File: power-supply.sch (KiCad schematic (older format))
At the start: 91 parts, among them IC1 TPS54561, J12 S2B-PH-K-S_LF__SN_, Q1 IRLML6402TRPBF, Q10 2N7002, Q11 2N7002, Q2 IRLML6402TRPBF, Q3 IRLML6402TRPBF, Q4 IRLML6402TRPBF, Q5 IRLML6402TRPBF, Q6 IRLML6402TRPBF, Q7 2N7002, Q8 2N7002, Q9 2N7002, U10 TPS62823DLCT, U11 TPS62823DLCT, U12 TPS62823DLCT, U13 TPS62823DLCT, U15 SN74LVC1G08DCKR, U16 SN74LS08DBR, U9 LM3881MME_NOPB

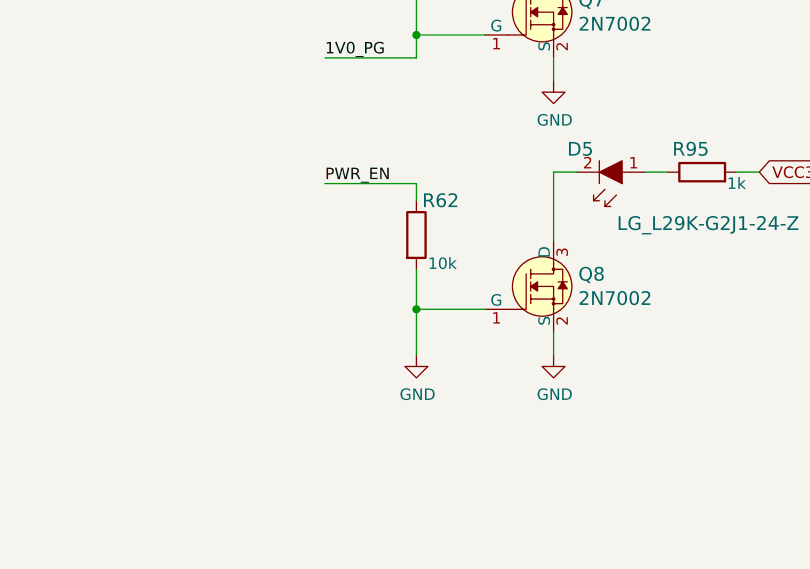
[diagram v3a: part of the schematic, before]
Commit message: Added power sequencer component placement, minor fixes in schematics
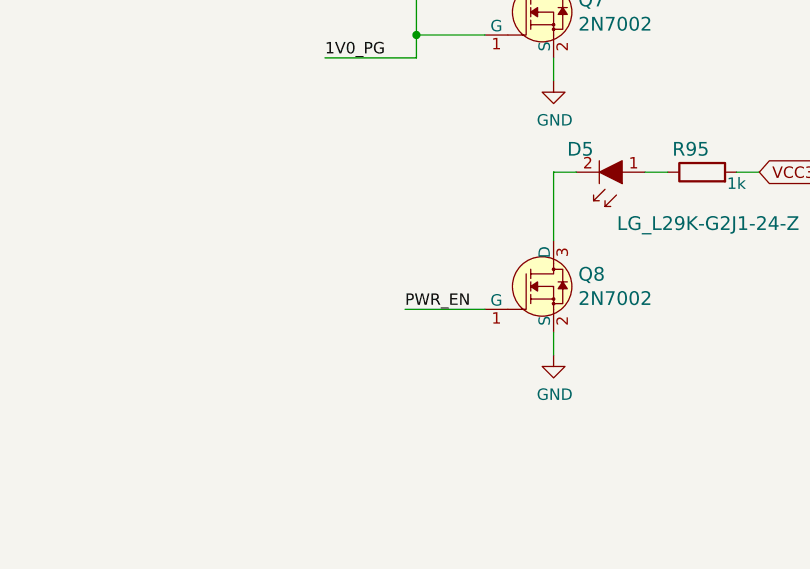
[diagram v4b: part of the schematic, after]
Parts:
- removed R62: R_10k_0402, artix-dc-scm-footprints:0402-res, symbol artix-dc-scm:R_10k_0402
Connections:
- wire segments 340 -> 336
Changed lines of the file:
@@
 AR Path="/5FD86BEB/60965625" Ref="U16"  Part="1"
 F 0 "U16" H 4175 9375 60  0000 C CNN
-F 1 "SN74LS08DBR" H 4050 9250 60  0000 C CNN
+F 1 "SN74LS08DBR" H 5250 9150 60  0000 C CNN
 F 2 "artix-dc-scm-footprints:SOP65P775X265-14N" H 4675 9075 60  0001 L CNN
 F 3 "http://www.ti.com/general/docs/suppproductinfo.tsp?distId=10&gotoUrl=http%3A%2F%2Fwww.ti.com%2Flit%2Fgpn%2Fsn74ls08" H 4675 9175 60  0001 L CNN
@@
 	10250 6775 10250 6675
 Wire Wire Line
-	9650 7775 9950 7775
-Wire Wire Line
 	10250 7175 10250 7475
-$Comp
-L artix-dc-scm:R_10k_0402 R62
-U 1 1 60986E26
-P 9650 7450
-F 0 "R62" V 9500 7475 60  0000 L CNN
-F 1 "R_10k_0402" H 9650 7300 60  0001 C CNN
-F 2 "artix-dc-scm-footprints:0402-res" H 9850 7650 60  0001 L CNN
-F 3 "" H 9650 7450 50  0001 C CNN
-F 4 "VISHAY" H 9850 7850 60  0001 L CNN "Manufacturer"
-F 5 "CRCW040210K0FKEDHP" H 9850 7750 60  0001 L CNN "MPN"
-F 6 "10k" V 9775 7500 50  0000 L CNN "Val"
-	1    9650 7450
-	0    1    1    0
-$EndComp
-Wire Wire Line
-	9650 7225 9650 7300
-Wire Wire Line
-	9650 7600 9650 7775
 $Comp
 L artix-dc-scm:LG_L29K-G2J1-24-Z D5
@@
 Wire Wire Line
 	11050 7175 11150 7175
-Connection ~ 9650 7775
 $Comp
 L artix-dc-scm:2N7002 Q8
@@
 Wire Wire Line
 	10250 7975 10250 7875
-Text Label 9250 7225 0    50   ~ 0
+Text Label 9600 7775 0    50   ~ 0
 PWR_EN
-Wire Wire Line
-	9250 7225 9650 7225
-$Comp
-L artix-dc-scm:GND #PWR0108
-U 1 1 60986E55
-P 9650 7975
-F 0 "#PWR0108" H 9650 7725 50  0001 C CNN
-F 1 "GND" H 9655 7802 50  0000 C CNN
-F 2 "" H 9650 7975 50  0001 C CNN
-F 3 "" H 9650 7975 50  0001 C CNN
-	1    9650 7975
-	1    0    0    -1
-$EndComp
-Wire Wire Line
-	9650 7775 9650 7975
 Wire Wire Line
 	9650 6575 9650 6675
@@
 Text GLabel 1125 9175 1    50   Input ~ 0
 VCC3V3
+Wire Wire Line
+	9950 7775 9600 7775
 $EndSCHEMATC

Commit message: Updated RoT and FLASH connections
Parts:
- renumbered R99 to R62
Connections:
- net labels added: ROT_RDY\ROT_GPIO0
- net labels removed: ROT_RDY
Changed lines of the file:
@@
 Text GLabel 4675 8875 2    50   Input ~ 0
 HPM_STBY_EN
-Text GLabel 4175 8775 0    50   Input ~ 0
-ROT_RDY
 Wire Wire Line
 	9725 2300 9650 2300
@@
 External 12V supply
 $Comp
-L artix-dc-scm:R_1k_0402 R99
+L artix-dc-scm:R_1k_0402 R62
 U 1 1 6003348A
 P 1125 9500
-F 0 "R99" V 1080 9570 60  0000 L CNN
+F 0 "R62" V 1080 9570 60  0000 L CNN
 F 1 "R_1k_0402" H 1125 9350 60  0001 C CNN
 F 2 "artix-dc-scm-footprints:0402-res" H 1325 9700 60  0001 L CNN
@@
 Wire Wire Line
 	9950 7775 9600 7775
+Text GLabel 4175 8775 0    50   Input ~ 0
+ROT_RDY\ROT_GPIO0
 $EndSCHEMATC

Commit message: Fixes after review (pin connections)
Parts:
- removed R77: R_124k_0402, artix-dc-scm-footprints:0402-res, symbol artix-dc-scm:R_124k_0402
- added R77: R_66k5_0402, antmicro-footprints:0402-res, symbol artix-dc-scm:R_66k5_0402
- added TP10, TP11, TP7, TP8, TP9: TP_SMD1MM, artix-dc-scm-footprints:Testpoint_smd_1mm, symbol artix-dc-scm:TP_SMD1MM
- U15: footprint artix-dc-scm-footprints:SC-70-5 -> antmicro-footprints:SC-70-5
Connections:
- wire segments 336 -> 333
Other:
- note removed: "SOURCE:LPDDR4 board"
- note removed: "TODO: calculate correct value for ??? resistor"
- note removed: "To CHECK"
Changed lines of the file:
@@
 Wire Wire Line
 	14325 2750 14625 2750
-Text Notes 14625 2300 0    50   ~ 0
+Text Notes 14600 2425 0    50   ~ 0
 3.3V/3A
 NoConn ~ -625 5725
@@
 Wire Wire Line
 	6600 3200 6600 3475
-Text GLabel 6600 2825 1    50   Input ~ 0
+Text GLabel 6600 2775 1    50   Input ~ 0
 VCC5V0
 Wire Wire Line
-	6600 2900 6600 2825
+	6600 2900 6600 2850
 $Comp
 L artix-dc-scm:WE_7447798720 L1
@@
 Wire Wire Line
 	12375 2750 12375 2800
-Text GLabel 12350 2350 0    50   Input ~ 0
-VCC5V0
-Wire Wire Line
-	12375 2350 12350 2350
 Wire Wire Line
 	12375 2350 12375 2750
@@
 Wire Wire Line
 	15275 3300 15275 3550
-Text GLabel 14925 2375 0    50   Input ~ 0
+Text GLabel 14975 2375 1    50   Input ~ 0
 VCC3V3
 Wire Wire Line
-	14975 2375 14925 2375
-Wire Wire Line
 	14975 2375 14975 2750
-Text Notes 4725 2725 0    50   ~ 0
-SOURCE:LPDDR4 board
 Text Notes 12725 3500 0    50   ~ 0
 SOURCE:Trelis board
@@
 Wire Wire Line
 	12400 4900 12400 4950
-Text GLabel 12375 4500 0    50   Input ~ 0
-VCC5V0
-Wire Wire Line
-	12400 4500 12375 4500
 Wire Wire Line
 	12400 4500 12400 4900
@@
 Wire Wire Line
 	15300 5450 15300 5700
-Text GLabel 14950 4525 0    50   Input ~ 0
+Text GLabel 15000 4525 1    50   Input ~ 0
 VCC1V8
-Wire Wire Line
-	15000 4525 14950 4525
 Wire Wire Line
 	15000 4525 15000 4900
@@
 Wire Wire Line
 	12450 6725 12450 6775
-Text GLabel 12425 6325 0    50   Input ~ 0
-VCC5V0
-Wire Wire Line
-	12450 6325 12425 6325
 Wire Wire Line
 	12450 6325 12450 6725
@@
 Wire Wire Line
 	15350 7275 15350 7525
-Text GLabel 15000 6350 0    50   Input ~ 0
+Text GLabel 15050 6350 1    50   Input ~ 0
 VCC1V35
-Wire Wire Line
-	15050 6350 15000 6350
 Wire Wire Line
 	15050 6350 15050 6725
@@
 	1    0    0    -1
 $EndComp
-Text Notes 1900 6825 0    118  ~ 0
-To CHECK
 Text Label 3000 9775 2    50   ~ 0
 VCCINT_EN
@@
 	1    0    0    -1
 $EndComp
-Text Notes 9075 975  0    118  ~ 0
+Text Notes 9525 1825 0    118  ~ 0
 PWR_LED Indicators
 Wire Notes Line
@@
 Wire Wire Line
 	15325 9000 15325 9250
-Text GLabel 14975 8075 0    50   Input ~ 0
+Text GLabel 15025 8075 1    50   Input ~ 0
 VCC1V0
-Wire Wire Line
-	15025 8075 14975 8075
 Wire Wire Line
 	15025 8075 15025 8450
@@
 Wire Wire Line
 	13875 8450 13825 8450
-$Comp
-L artix-dc-scm:R_124k_0402 R77
-U 1 1 63A59281
-P 14675 8675
-F 0 "R77" V 14630 8745 60  0000 L CNN
-F 1 "R_124k_0402" H 14675 8525 60  0001 C CNN
-F 2 "artix-dc-scm-footprints:0402-res" H 14875 8875 60  0001 L CNN
-F 3 "" H 14675 8675 50  0001 C CNN
-F 4 "WALSIN" H 14875 9075 60  0001 L CNN "Manufacturer"
-F 5 "WR04X1243FTL" H 14875 8975 60  0001 L CNN "MPN"
-F 6 "???" V 14728 8745 50  0000 L CNN "Val"
-	1    14675 8675
-	0    1    1    0
-$EndComp
-Text Notes 14125 9400 0    50   ~ 0
-TODO: calculate correct value for ??? resistor
 Text Notes 4300 11025 0    50   ~ 0
 STEP1: VRs start and RoT boots (HPM_STBY_EN when both are done)\nSTEP2: HPM starts its VRs and sets HPM_STBY_RDY when done\nSTEP3: FPGA VCCINT (1.0V)\nSTEP4: FPGA VCCAUX + DDR3 (1.8V, 1.35V)\nSTEP5: FPGA VCCIO + DDR3 (3.3V, DDRVTT), HPM reset is de-asserted\nSTEP6: HPM boots
@@
 F 0 "U15" H 4625 7250 60  0000 L CNN
 F 1 "SN74LVC1G08DCKR" H 4550 7150 60  0000 L CNN
-F 2 "artix-dc-scm-footprints:SC-70-5" H 4675 7650 60  0001 L CNN
+F 2 "antmicro-footprints:SC-70-5" H 4675 7650 60  0001 L CNN
 F 3 "http://www.ti.com/general/docs/suppproductinfo.tsp?distId=10&gotoUrl=http%3A%2F%2Fwww.ti.com%2Flit%2Fgpn%2Fsn74lvc1g08" H 4675 7750 60  0001 L CNN
 F 4 "SN74LVC1G08DCKR" H 4675 7950 60  0001 L CNN "MPN"
@@
 	1    0    0    -1
 $EndComp
-Text GLabel 9650 2300 0    50   Input ~ 0
-VCC3V3
-Text GLabel 9625 3525 0    50   Input ~ 0
-VCC1V8
-Text GLabel 9625 4750 0    50   Input ~ 0
-VCC1V35
 Text Label 9300 5400 0    50   ~ 0
 1V35_PG
@@
 	1    0    0    -1
 $EndComp
-Text GLabel 9575 6025 0    50   Input ~ 0
-VCC1V0
 $Comp
 L artix-dc-scm:GND #PWR0106
@@
 Text GLabel 4175 8775 0    50   Input ~ 0
 ROT_RDY\ROT_GPIO0
+$Comp
+L artix-dc-scm:R_66k5_0402 R77
+U 1 1 61771C2F
+P 14675 8675
+F 0 "R77" V 14630 8745 60  0000 L CNN
+F 1 "R_66k5_0402" H 14675 8525 60  0001 C CNN
+F 2 "antmicro-footprints:0402-res" H 14875 8875 60  0001 L CNN
+F 3 "" H 14675 8675 50  0001 C CNN
+F 4 "PANASONIC" H 14875 9075 60  0001 L CNN "Manufacturer"
+F 5 "ERJ2RKF6652X" H 14875 8975 60  0001 L CNN "MPN"
+F 6 "66k5" V 14728 8745 50  0000 L CNN "Val"
+	1    14675 8675
+	0    1    1    0
+$EndComp
+Text GLabel 9650 2300 0    50   Input ~ 0
+VCC5V0
+Text GLabel 9625 3525 0    50   Input ~ 0
+VCC5V0
+Text GLabel 9625 4750 0    50   Input ~ 0
+VCC5V0
+Text GLabel 9575 6025 0    50   Input ~ 0
+VCC5V0
+$Comp
+L artix-dc-scm:TP_SMD1MM TP8
+U 1 1 617CB838
+P 15375 2750
+F 0 "TP8" V 15280 2797 50  0000 C CNN
+F 1 "TP_SMD1MM" H 15375 2650 50  0001 C CNN
+F 2 "artix-dc-scm-footprints:Testpoint_smd_1mm" H 15575 2950 60  0001 L CNN
+F 3 "" H 15575 3050 60  0001 L CNN
+	1    15375 2750
+	0    -1   -1   0
+$EndComp
+Connection ~ 15275 2750
+$Comp
+L artix-dc-scm:TP_SMD1MM TP9
+U 1 1 61819AA7
+P 15400 4900
+F 0 "TP9" V 15305 4947 50  0000 C CNN
+F 1 "TP_SMD1MM" H 15400 4800 50  0001 C CNN
+F 2 "artix-dc-scm-footprints:Testpoint_smd_1mm" H 15600 5100 60  0001 L CNN
+F 3 "" H 15600 5200 60  0001 L CNN
+	1    15400 4900
+	0    -1   -1   0
+$EndComp
+Connection ~ 15300 4900
+$Comp
+L artix-dc-scm:TP_SMD1MM TP11
+U 1 1 61841199
+P 15450 6725
+F 0 "TP11" V 15355 6772 50  0000 C CNN
+F 1 "TP_SMD1MM" H 15450 6625 50  0001 C CNN
+F 2 "artix-dc-scm-footprints:Testpoint_smd_1mm" H 15650 6925 60  0001 L CNN
+F 3 "" H 15650 7025 60  0001 L CNN
+	1    15450 6725
+	0    -1   -1   0
+$EndComp
+Connection ~ 15350 6725
+$Comp
+L artix-dc-scm:TP_SMD1MM TP10
+U 1 1 618652F8
+P 15425 8450
+F 0 "TP10" V 15330 8497 50  0000 C CNN
+F 1 "TP_SMD1MM" H 15425 8350 50  0001 C CNN
+F 2 "artix-dc-scm-footprints:Testpoint_smd_1mm" H 15625 8650 60  0001 L CNN
+F 3 "" H 15625 8750 60  0001 L CNN
+	1    15425 8450
+	0    -1   -1   0
+$EndComp
+Connection ~ 15325 8450
+$Comp
+L artix-dc-scm:TP_SMD1MM TP7
+U 1 1 61885323
+P 6700 2850
+F 0 "TP7" V 6675 2700 50  0000 C CNN
+F 1 "TP_SMD1MM" H 6700 2750 50  0001 C CNN
+F 2 "artix-dc-scm-footprints:Testpoint_smd_1mm" H 6900 3050 60  0001 L CNN
+F 3 "" H 6900 3150 60  0001 L CNN
+	1    6700 2850
+	0    -1   -1   0
+$EndComp
+Connection ~ 6600 2850
+Wire Wire Line
+	6600 2850 6600 2775
+Wire Wire Line
+	12450 6325 12425 6325
+Text GLabel 12425 6325 0    50   Input ~ 0
+VCC5V0
+Wire Wire Line
+	12400 4500 12375 4500
+Text GLabel 12375 4500 0    50   Input ~ 0
+VCC5V0
+Wire Wire Line
+	12375 2350 12350 2350
+Text GLabel 12350 2350 0    50   Input ~ 0
+VCC5V0
 $EndSCHEMATC

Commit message: Added USB client chip
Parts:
- added C14, C15, C16: C_10u_25V_0603, antmicro-footprints:0603-cap, symbol antmicroCapacitors0603:C_10u_25V_0603
- added C17: C_100n_0402_16V, antmicro-footprints:0402-cap, symbol antmicroCapacitorsmisc:C_100n_0402_16V
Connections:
- wire segments 333 -> 349
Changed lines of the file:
@@
 Text GLabel 12350 2350 0    50   Input ~ 0
 VCC5V0
+$Comp
+L antmicroCapacitors0603:C_10u_25V_0603 C14
+U 1 1 619949C4
+P 3200 1675
+F 0 "C14" H 3315 1720 60  0000 L CNN
+F 1 "C_10u_25V_0603" H 3200 1525 60  0001 C CNN
+F 2 "antmicro-footprints:0603-cap" H 3400 1875 60  0001 L CNN
+F 3 "" H 3200 1675 50  0001 C CNN
+F 4 "TDK" H 3400 2075 60  0001 L CNN "Manufacturer"
+F 5 "C1608X5R1E106M080AC" H 3400 1975 60  0001 L CNN "MPN"
+F 6 "10u/25V" H 3315 1622 50  0000 L CNN "Val"
+	1    3200 1675
+	1    0    0    -1
+$EndComp
+$Comp
+L antmicroCapacitors0603:C_10u_25V_0603 C15
+U 1 1 619975A1
+P 3475 1675
+F 0 "C15" H 3590 1720 60  0000 L CNN
+F 1 "C_10u_25V_0603" H 3475 1525 60  0001 C CNN
+F 2 "antmicro-footprints:0603-cap" H 3675 1875 60  0001 L CNN
+F 3 "" H 3475 1675 50  0001 C CNN
+F 4 "TDK" H 3675 2075 60  0001 L CNN "Manufacturer"
+F 5 "C1608X5R1E106M080AC" H 3675 1975 60  0001 L CNN "MPN"
+F 6 "10u/25V" H 3590 1622 50  0000 L CNN "Val"
+	1    3475 1675
+	1    0    0    -1
+$EndComp
+$Comp
+L antmicroCapacitors0603:C_10u_25V_0603 C16
+U 1 1 619977B0
+P 3750 1675
+F 0 "C16" H 3865 1720 60  0000 L CNN
+F 1 "C_10u_25V_0603" H 3750 1525 60  0001 C CNN
+F 2 "antmicro-footprints:0603-cap" H 3950 1875 60  0001 L CNN
+F 3 "" H 3750 1675 50  0001 C CNN
+F 4 "TDK" H 3950 2075 60  0001 L CNN "Manufacturer"
+F 5 "C1608X5R1E106M080AC" H 3950 1975 60  0001 L CNN "MPN"
+F 6 "10u/25V" H 3865 1622 50  0000 L CNN "Val"
+	1    3750 1675
+	1    0    0    -1
+$EndComp
+$Comp
+L antmicroCapacitorsmisc:C_100n_0402_16V C17
+U 1 1 619982FA
+P 4025 1675
+F 0 "C17" H 4140 1720 60  0000 L CNN
+F 1 "C_100n_0402_16V" H 4025 1525 60  0001 C CNN
+F 2 "antmicro-footprints:0402-cap" H 4225 1875 60  0001 L CNN
+F 3 "" H 4025 1675 50  0001 C CNN
+F 4 "MULTICOMP" H 4225 2075 60  0001 L CNN "Manufacturer"
+F 5 "MC0402B104K160CT" H 4225 1975 60  0001 L CNN "MPN"
+F 6 "100n" H 4140 1622 50  0000 L CNN "Val"
+	1    4025 1675
+	1    0    0    -1
+$EndComp
+Text GLabel 3200 1375 1    50   Input ~ 0
+VCC12V
+$Comp
+L artix-dc-scm:GND #PWR092
+U 1 1 619DB17E
+P 3200 2000
+F 0 "#PWR092" H 3200 1750 50  0001 C CNN
+F 1 "GND" H 3205 1827 50  0000 C CNN
+F 2 "" H 3200 2000 50  0001 C CNN
+F 3 "" H 3200 2000 50  0001 C CNN
+	1    3200 2000
+	1    0    0    -1
+$EndComp
+Wire Wire Line
+	3200 1375 3200 1450
+Wire Wire Line
+	3200 1825 3200 1900
+Wire Wire Line
+	3200 1450 3475 1450
+Wire Wire Line
+	4025 1450 4025 1525
+Connection ~ 3200 1450
+Wire Wire Line
+	3200 1450 3200 1525
+Wire Wire Line
+	3750 1525 3750 1450
+Connection ~ 3750 1450
+Wire Wire Line
+	3750 1450 4025 1450
+Wire Wire Line
+	3475 1525 3475 1450
+Connection ~ 3475 1450
+Wire Wire Line
+	3475 1450 3750 1450
+Wire Wire Line
+	3475 1825 3475 1900
+Wire Wire Line
+	3475 1900 3200 1900
+Connection ~ 3200 1900
+Wire Wire Line
+	3200 1900 3200 2000
+Wire Wire Line
+	4025 1825 4025 1900
+Wire Wire Line
+	4025 1900 3750 1900
+Connection ~ 3475 1900
+Wire Wire Line
+	3750 1825 3750 1900
+Connection ~ 3750 1900
+Wire Wire Line
+	3750 1900 3475 1900
 $EndSCHEMATC

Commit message: Added local libs
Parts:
- C14, C15, C16: symbol antmicroCapacitors0603:C_10u_25V_0603 -> artix-dc-scm:C_10u_25V_0603
- C17: symbol antmicroCapacitorsmisc:C_100n_0402_16V -> artix-dc-scm:C_100n_0402_16V
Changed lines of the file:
@@
 VCC5V0
 $Comp
-L antmicroCapacitors0603:C_10u_25V_0603 C14
+L artix-dc-scm:C_10u_25V_0603 C14
 U 1 1 619949C4
 P 3200 1675
@@
 $EndComp
 $Comp
-L antmicroCapacitors0603:C_10u_25V_0603 C15
+L artix-dc-scm:C_10u_25V_0603 C15
 U 1 1 619975A1
 P 3475 1675
@@
 $EndComp
 $Comp
-L antmicroCapacitors0603:C_10u_25V_0603 C16
+L artix-dc-scm:C_10u_25V_0603 C16
 U 1 1 619977B0
 P 3750 1675
@@
 $EndComp
 $Comp
-L antmicroCapacitorsmisc:C_100n_0402_16V C17
+L artix-dc-scm:C_100n_0402_16V C17
 U 1 1 619982FA
 P 4025 1675
